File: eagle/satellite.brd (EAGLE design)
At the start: 80 x 78.7 mm, 10 parts

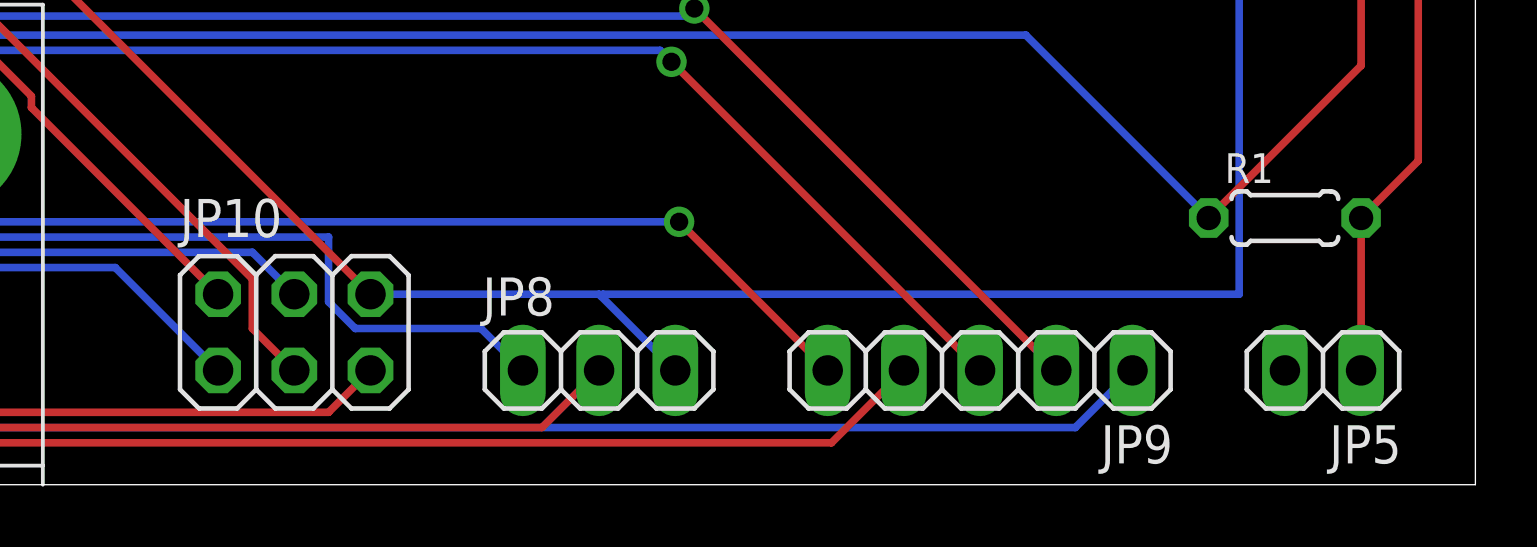
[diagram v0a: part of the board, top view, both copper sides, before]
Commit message: eagle file changes that were submitted for a quote
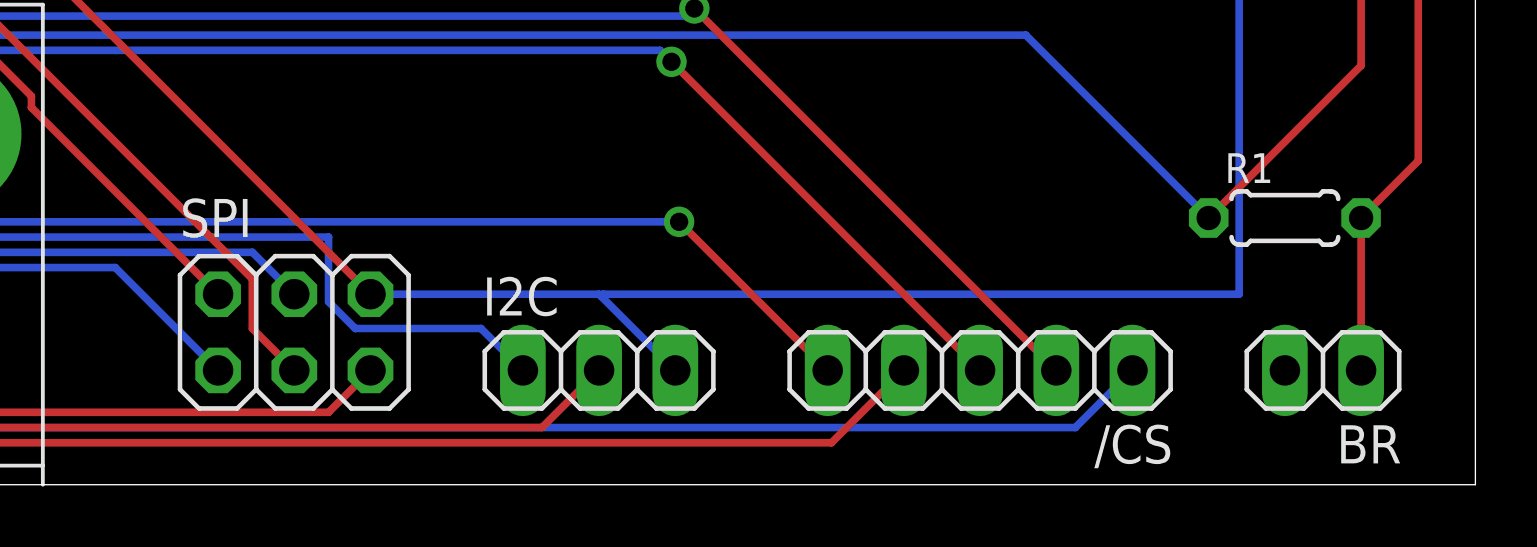
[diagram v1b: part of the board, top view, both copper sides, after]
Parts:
- renumbered JP10 to SPI, JP5 to BR, JP8 to I2C, JP9 to /CS
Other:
- board text added: "ADAM CHASE 07/29/2013 PRESSURE BOARD v1.00"
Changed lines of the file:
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@@
 <rectangle x1="7.62" y1="21.59" x2="36.83" y2="48.26" layer="42"/>
 <rectangle x1="41.91" y1="21.59" x2="71.12" y2="48.26" layer="42"/>
+<text x="39.37" y="48.26" size="1.778" layer="22" rot="MR0" align="center">ADAM CHASE
+07/29/2013
+PRESSURE BOARD
+v1.00</text>
 </plain>
 <attributes>
@@
 <element name="JP4" library="pinhead" package="1X06" value="" x="3.81" y="35.56" rot="R90"/>
 <element name="R1" library="rcl" package="0204/5" value="4.7K" x="73.66" y="8.89"/>
-<element name="JP5" library="pinhead" package="1X02" value="" x="74.93" y="3.81" rot="R180"/>
-<element name="JP8" library="pinhead" package="1X03" value="" x="50.8" y="3.81"/>
-<element name="JP9" library="pinhead" package="1X05" value="" x="63.5" y="3.81" rot="R180"/>
-<element name="JP10" library="pinhead" package="2X03" value="" x="40.64" y="5.08"/>
+<element name="BR" library="pinhead" package="1X02" value="" x="74.93" y="3.81" smashed="yes" rot="R180">
+<attribute name="NAME" x="77.5462" y="1.9812" size="1.27" layer="25" ratio="10" rot="R180"/>
+<attribute name="VALUE" x="77.47" y="6.985" size="1.27" layer="27" rot="R180"/>
+</element>
+<element name="I2C" library="pinhead" package="1X03" value="" x="50.8" y="3.81" smashed="yes">
+<attribute name="NAME" x="46.9138" y="5.6388" size="1.27" layer="25" ratio="10"/>
+<attribute name="VALUE" x="46.99" y="0.635" size="1.27" layer="27"/>
+</element>
+<element name="/CS" library="pinhead" package="1X05" value="" x="63.5" y="3.81" rot="R180"/>
+<element name="SPI" library="pinhead" package="2X03" value="" x="40.64" y="5.08" smashed="yes">
+<attribute name="NAME" x="36.83" y="8.255" size="1.27" layer="25" ratio="10"/>
+<attribute name="VALUE" x="36.83" y="0.635" size="1.27" layer="27"/>
+</element>
 </elements>
 <signals>
@@
 <signal name="SCLK">
 <contactref element="VGA1" pad="4"/>
-<contactref element="JP10" pad="3"/>
+<contactref element="SPI" pad="3"/>
 <wire x1="39.243" y1="5.207" x2="40.64" y2="3.81" width="0.254" layer="1"/>
 <wire x1="39.243" y1="6.858" x2="39.243" y2="5.207" width="0.254" layer="1"/>
@@
 <contactref element="JP4" pad="5"/>
 <contactref element="R1" pad="2"/>
-<contactref element="JP5" pad="1"/>
+<contactref element="BR" pad="1"/>
 <wire x1="7.112" y1="42.672" x2="3.81" y2="39.37" width="0.254" layer="16"/>
 <wire x1="6.731" y1="43.053" x2="7.112" y2="42.672" width="0.254" layer="1"/>
@@
 <contactref element="VGA1" pad="1"/>
 <contactref element="R1" pad="1"/>
-<contactref element="JP10" pad="2"/>
+<contactref element="SPI" pad="2"/>
 <wire x1="76.2" y1="13.97" x2="71.12" y2="8.89" width="0.254" layer="1"/>
 <wire x1="76.2" y1="29.21" x2="76.2" y2="13.97" width="0.254" layer="1"/>
@@
 <signal name="MISO">
 <contactref element="VGA1" pad="12"/>
-<contactref element="JP10" pad="1"/>
+<contactref element="SPI" pad="1"/>
 <wire x1="34.671" y1="7.239" x2="38.1" y2="3.81" width="0.254" layer="16"/>
 <wire x1="20.447" y1="7.239" x2="34.671" y2="7.239" width="0.254" layer="16"/>
@@
 <signal name="SDA">
 <contactref element="VGA1" pad="8"/>
-<contactref element="JP8" pad="1"/>
+<contactref element="I2C" pad="1"/>
 <wire x1="46.863" y1="5.207" x2="48.26" y2="3.81" width="0.254" layer="16"/>
 <wire x1="42.672" y1="5.207" x2="46.863" y2="5.207" width="0.254" layer="16"/>
@@
 <signal name="SCL">
 <contactref element="VGA1" pad="7"/>
-<contactref element="JP8" pad="2"/>
+<contactref element="I2C" pad="2"/>
 <wire x1="48.895" y1="1.905" x2="50.8" y2="3.81" width="0.254" layer="1"/>
 <wire x1="22.098" y1="1.905" x2="48.895" y2="1.905" width="0.254" layer="1"/>
@@
 <signal name="GPIO5">
 <contactref element="VGA1" pad="6"/>
-<contactref element="JP9" pad="5"/>
+<contactref element="/CS" pad="5"/>
 <wire x1="53.467" y1="8.763" x2="58.42" y2="3.81" width="0.254" layer="1"/>
 <wire x1="24.892" y1="8.763" x2="53.467" y2="8.763" width="0.254" layer="16"/>
@@
 <signal name="GPIO2">
 <contactref element="VGA1" pad="5"/>
-<contactref element="JP9" pad="2"/>
+<contactref element="/CS" pad="2"/>
 <wire x1="53.975" y1="15.875" x2="66.04" y2="3.81" width="0.254" layer="1"/>
 <wire x1="53.721" y1="15.621" x2="53.975" y2="15.875" width="0.254" layer="16"/>
@@
 <signal name="GPIO3">
 <contactref element="VGA1" pad="9"/>
-<contactref element="JP9" pad="3"/>
+<contactref element="/CS" pad="3"/>
 <wire x1="53.213" y1="14.097" x2="63.5" y2="3.81" width="0.254" layer="1"/>
 <wire x1="52.832" y1="14.478" x2="53.213" y2="14.097" width="0.254" layer="16"/>
@@
 <signal name="GPIO1">
 <contactref element="VGA1" pad="15"/>
-<contactref element="JP9" pad="1"/>
+<contactref element="/CS" pad="1"/>
 <wire x1="66.675" y1="1.905" x2="68.58" y2="3.81" width="0.254" layer="16"/>
 <wire x1="18.923" y1="1.905" x2="66.675" y2="1.905" width="0.254" layer="16"/>
@@
 <signal name="GPIO4">
 <contactref element="VGA1" pad="10"/>
-<contactref element="JP9" pad="4"/>
+<contactref element="/CS" pad="4"/>
 <wire x1="58.547" y1="1.397" x2="60.96" y2="3.81" width="0.254" layer="1"/>
 <wire x1="10.414" y1="1.397" x2="58.547" y2="1.397" width="0.254" layer="1"/>
@@
 <signal name="MOSI">
 <contactref element="VGA1" pad="11"/>
-<contactref element="JP10" pad="4"/>
+<contactref element="SPI" pad="4"/>
 <wire x1="39.243" y1="7.747" x2="40.64" y2="6.35" width="0.254" layer="16"/>
 <wire x1="22.225" y1="7.747" x2="39.243" y2="7.747" width="0.254" layer="16"/>
@@
 <contactref element="JP3" pad="4"/>
 <contactref element="JP4" pad="4"/>
-<contactref element="JP10" pad="6"/>
-<contactref element="JP8" pad="3"/>
+<contactref element="SPI" pad="6"/>
+<contactref element="I2C" pad="3"/>
 <wire x1="74.295" y1="38.735" x2="76.2" y2="36.83" width="0.254" layer="1"/>
 <wire x1="74.295" y1="40.005" x2="74.295" y2="38.735" width="0.254" layer="1"/>
@@
 <signal name="33V">
 <contactref element="VGA1" pad="2"/>
-<contactref element="JP10" pad="5"/>
+<contactref element="SPI" pad="5"/>
 <wire x1="41.783" y1="2.413" x2="43.18" y2="3.81" width="0.254" layer="1"/>
 <wire x1="23.241" y1="2.413" x2="41.783" y2="2.413" width="0.254" layer="1"/>
@@
 </board>
 </drawing>
+<compatibility>
+<note version="6.3" minversion="6.2.2" severity="warning">
+Since Version 6.2.2 text objects can contain more than one line,
+which will not be processed correctly with this version.
+</note>
+</compatibility>
 </eagle>

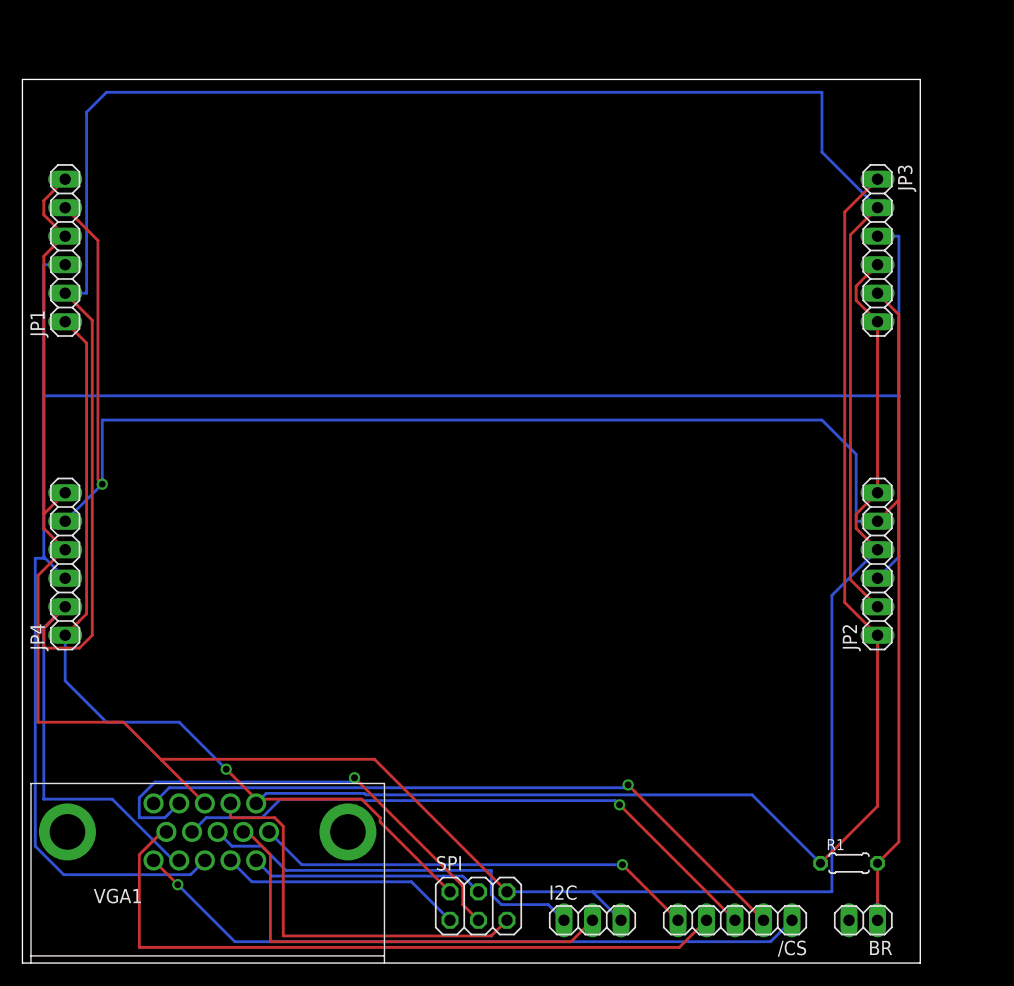
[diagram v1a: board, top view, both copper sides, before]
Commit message: modified satellite board to fix incorrect routing
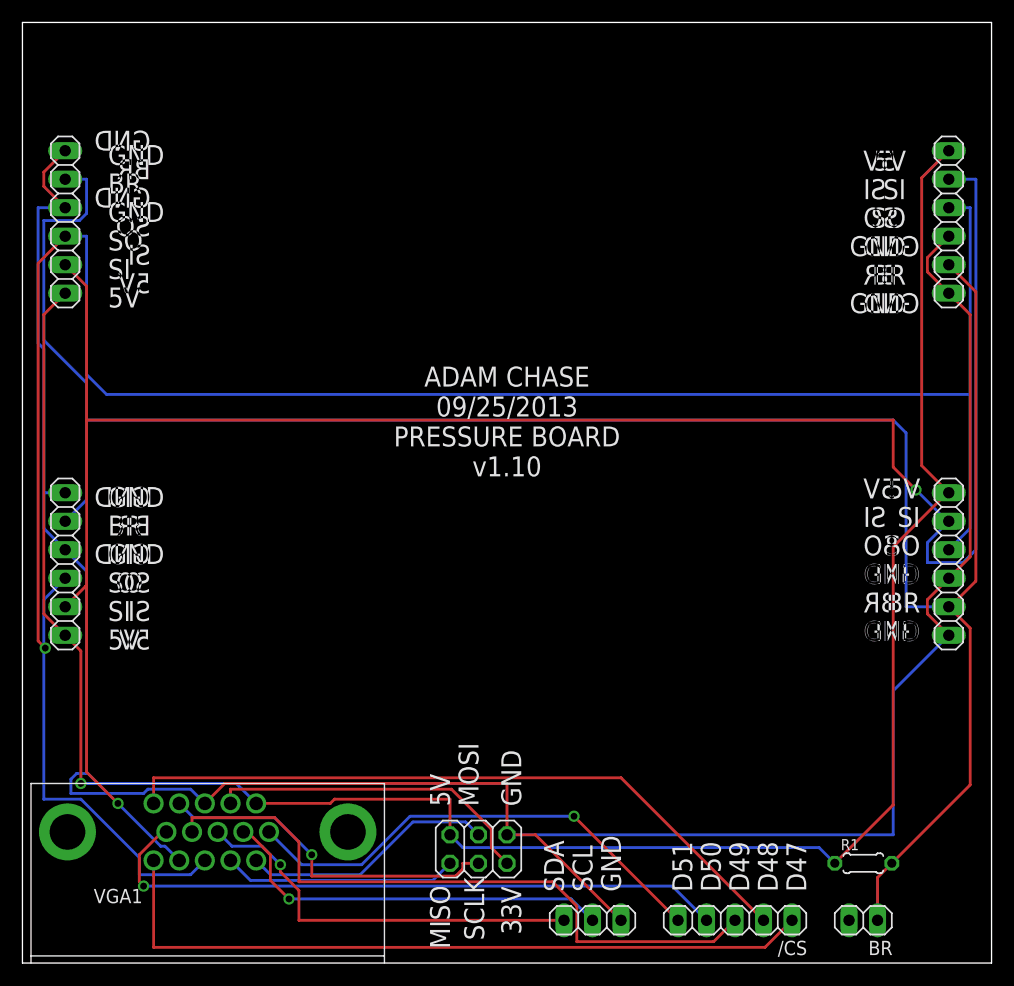
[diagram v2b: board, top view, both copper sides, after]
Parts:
- moved JP3 6.84 mm to (82.5, 66.0)
- moved JP2 6.35 mm to (82.5, 35.6), turned to 270 degrees
- moved SPI 5.08 mm to (40.6, 10.2)
- moved JP1 2.54 mm to (3.81, 66.0)
- moved R1 1.27 mm to (74.9, 8.89)
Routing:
- net BR: track 172.8 -> 195.7 mm, vias 1 -> 0
- net RX: track 183.2 -> 204.0 mm, vias 0 -> 1
- net TX: track 207.2 -> 187.9 mm, vias 0 -> 2
- net GND: track 202.2 -> 218.8 mm
- net SCLK: track 43.1 -> 31.2 mm
- net 5V: track 195.0 -> 187.9 mm
- net 33V: track 36.6 -> 29.6 mm
- net GPIO4: track 63.1 -> 57.6 mm, vias 0 -> 1
- net GPIO1: track 60.7 -> 65.6 mm, vias 1 -> 0
- net GPIO3: track 54.1 -> 59.0 mm, vias 1 -> 0
- net SCL: track 40.5 -> 35.7 mm, vias 0 -> 1
- net GPIO5: track 39.7 -> 43.3 mm
- net GPIO2: track 60.0 -> 61.9 mm, vias 1 -> 0
- net MOSI: track 21.0 -> 22.8 mm
- net MISO: track 21.8 -> 20.9 mm
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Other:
- board size 80 x 78.7 mm -> 86.4 x 83.8 mm
- board text added: "33V"
- board text added: "5V"
- board text added: "ADAM CHASE 09/25/2013 PRESSURE BOARD v1.10"
- board text added: "BR"
- board text added: "BR JUMPER ON = 19200 OFF = 9600"
- board text added: "D47"
- board text added: "D48"
- board text added: "D49"
- board text added: "D50"
- board text added: "D51"
- board text added: "GND"
- board text added: "MISO"
- board text added: "MOSI"
- board text added: "SCL"
- board text added: "SCLK"
- board text added: "SDA"
- board text added: "SI"
- board text added: "SO"
- board text removed: "ADAM CHASE 07/29/2013 PRESSURE BOARD v1.00"
